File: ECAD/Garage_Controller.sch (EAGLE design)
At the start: 91 parts, among them IC1 LM358D, IC2 LM358D, J1 1885410000, J2 1885410000, J3 1885430000, J4 1885430000, J5 1885430000, J6 1885430000, J7 1885430000, Q1 35A/25V/8.5mΩ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

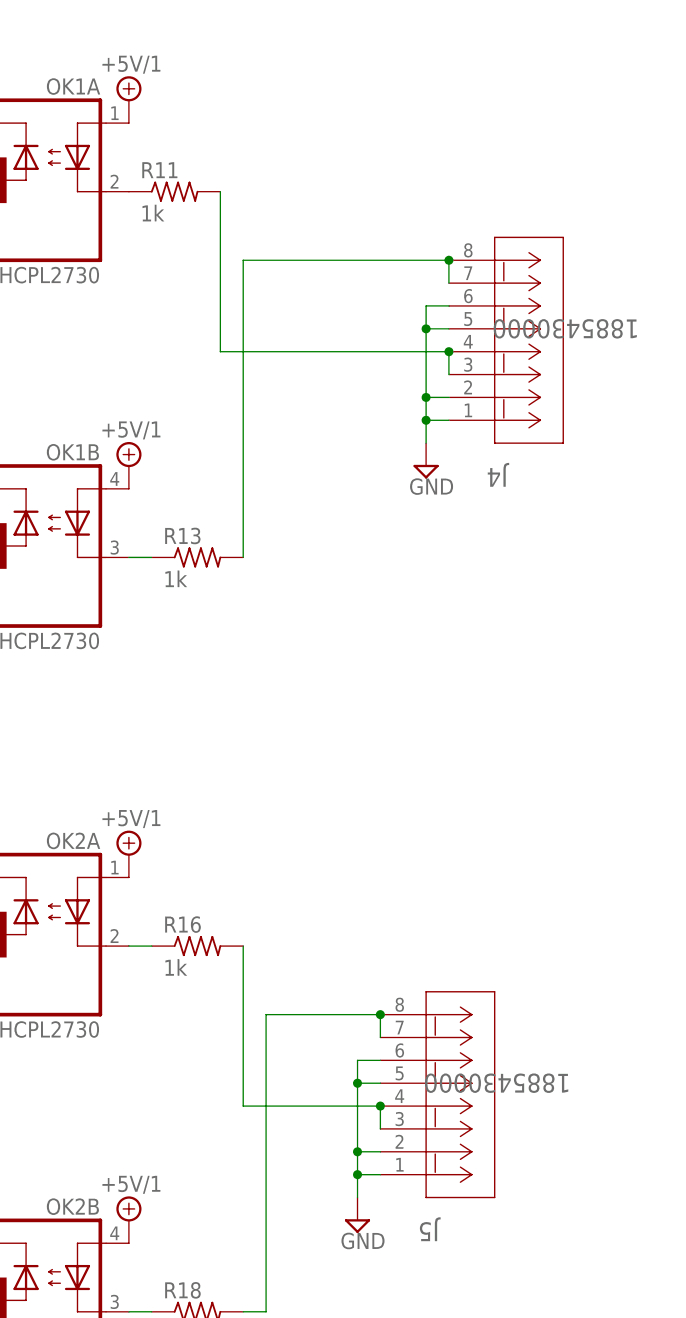
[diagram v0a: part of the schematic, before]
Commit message: Providing +5V at DI connector
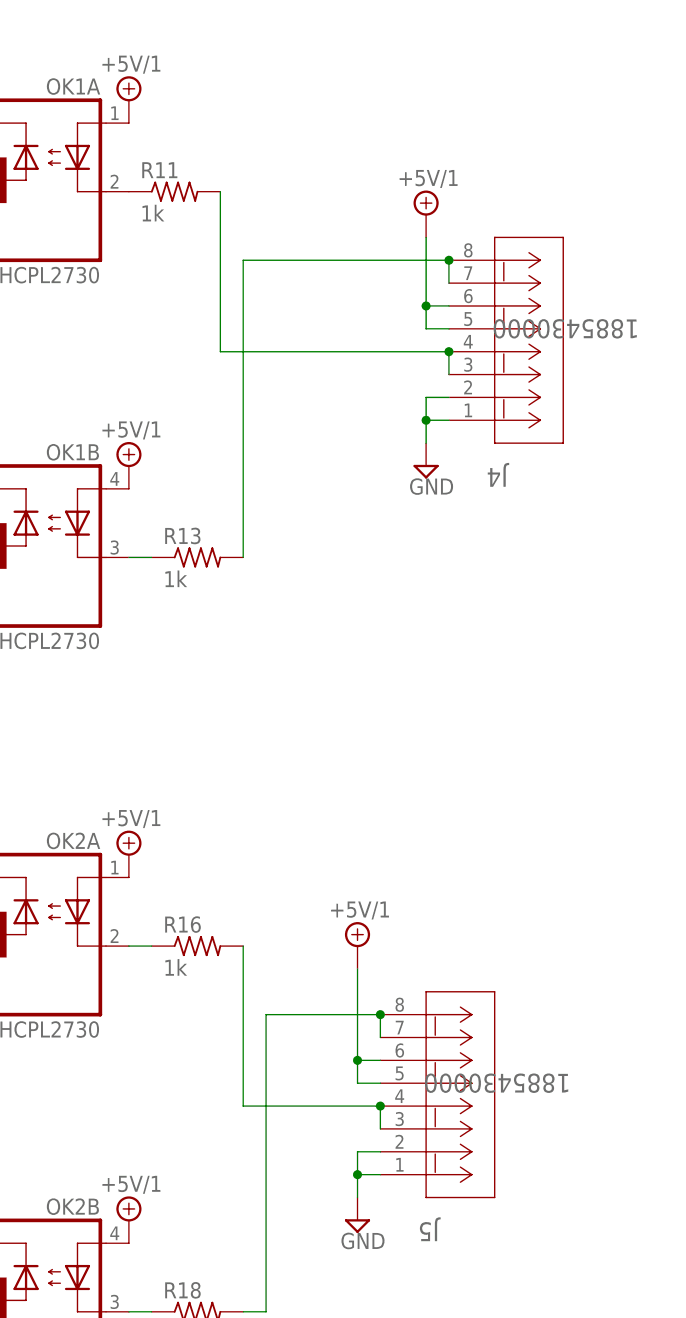
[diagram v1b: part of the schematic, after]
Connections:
- net +5V/1: now also J4.5, J4.6, J5.5, J5.6
- net GND: no longer J4.5, J4.6, J5.5, J5.6
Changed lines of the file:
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@@
 <part name="SUPPLY45" library="supply2" deviceset="GND" device=""/>
 <part name="SUPPLY46" library="supply2" deviceset="+5V" device=""/>
+<part name="SUPPLY47" library="supply2" deviceset="+5V/1" device=""/>
+<part name="SUPPLY48" library="supply2" deviceset="+5V/1" device=""/>
 </parts>
 <sheets>
@@
 <instance part="SUPPLY45" gate="GND" x="297.18" y="175.26"/>
 <instance part="SUPPLY46" gate="+5V" x="297.18" y="198.12"/>
+<instance part="SUPPLY47" gate="G$1" x="325.12" y="-53.34"/>
+<instance part="SUPPLY48" gate="G$1" x="317.5" y="-134.62"/>
 </instances>
 <busses>
@@
 <wire x1="325.12" y1="-73.66" x2="325.12" y2="-76.2" width="0.1524" layer="91"/>
 <junction x="325.12" y="-76.2"/>
-<pinref part="J4" gate="A" pin="5"/>
-<wire x1="327.66" y1="-66.04" x2="325.12" y2="-66.04" width="0.1524" layer="91"/>
-<wire x1="325.12" y1="-66.04" x2="325.12" y2="-73.66" width="0.1524" layer="91"/>
-<junction x="325.12" y="-73.66"/>
-<pinref part="J4" gate="A" pin="6"/>
-<wire x1="327.66" y1="-63.5" x2="325.12" y2="-63.5" width="0.1524" layer="91"/>
-<wire x1="325.12" y1="-63.5" x2="325.12" y2="-66.04" width="0.1524" layer="91"/>
-<junction x="325.12" y="-66.04"/>
 </segment>
 <segment>
@@
 <wire x1="317.5" y1="-157.48" x2="317.5" y2="-160.02" width="0.1524" layer="91"/>
 <junction x="317.5" y="-160.02"/>
-<pinref part="J5" gate="A" pin="5"/>
-<wire x1="320.04" y1="-149.86" x2="317.5" y2="-149.86" width="0.1524" layer="91"/>
-<wire x1="317.5" y1="-149.86" x2="317.5" y2="-157.48" width="0.1524" layer="91"/>
-<junction x="317.5" y="-157.48"/>
-<pinref part="J5" gate="A" pin="6"/>
-<wire x1="320.04" y1="-147.32" x2="317.5" y2="-147.32" width="0.1524" layer="91"/>
-<wire x1="317.5" y1="-147.32" x2="317.5" y2="-149.86" width="0.1524" layer="91"/>
-<junction x="317.5" y="-149.86"/>
 </segment>
 <segment>
@@
 <pinref part="SUPPLY44" gate="G$1" pin="+5V/1"/>
 </segment>
-</net>
+<segment>
+<pinref part="J4" gate="A" pin="5"/>
+<wire x1="327.66" y1="-66.04" x2="325.12" y2="-66.04" width="0.1524" layer="91"/>
+<pinref part="J4" gate="A" pin="6"/>
+<wire x1="327.66" y1="-63.5" x2="325.12" y2="-63.5" width="0.1524" layer="91"/>
+<wire x1="325.12" y1="-63.5" x2="325.12" y2="-66.04" width="0.1524" layer="91"/>
+<pinref part="SUPPLY47" gate="G$1" pin="+5V/1"/>
+<wire x1="325.12" y1="-63.5" x2="325.12" y2="-55.88" width="0.1524" layer="91"/>
+<junction x="325.12" y="-63.5"/>
+</segment>
+<segment>
+<pinref part="J5" gate="A" pin="5"/>
+<wire x1="320.04" y1="-149.86" x2="317.5" y2="-149.86" width="0.1524" layer="91"/>
+<pinref part="J5" gate="A" pin="6"/>
+<wire x1="320.04" y1="-147.32" x2="317.5" y2="-147.32" width="0.1524" layer="91"/>
+<wire x1="317.5" y1="-147.32" x2="317.5" y2="-149.86" width="0.1524" layer="91"/>
+<pinref part="SUPPLY48" gate="G$1" pin="+5V/1"/>
+<wire x1="317.5" y1="-147.32" x2="317.5" y2="-137.16" width="0.1524" layer="91"/>
+<junction x="317.5" y="-147.32"/>
+</segment>
+</net>

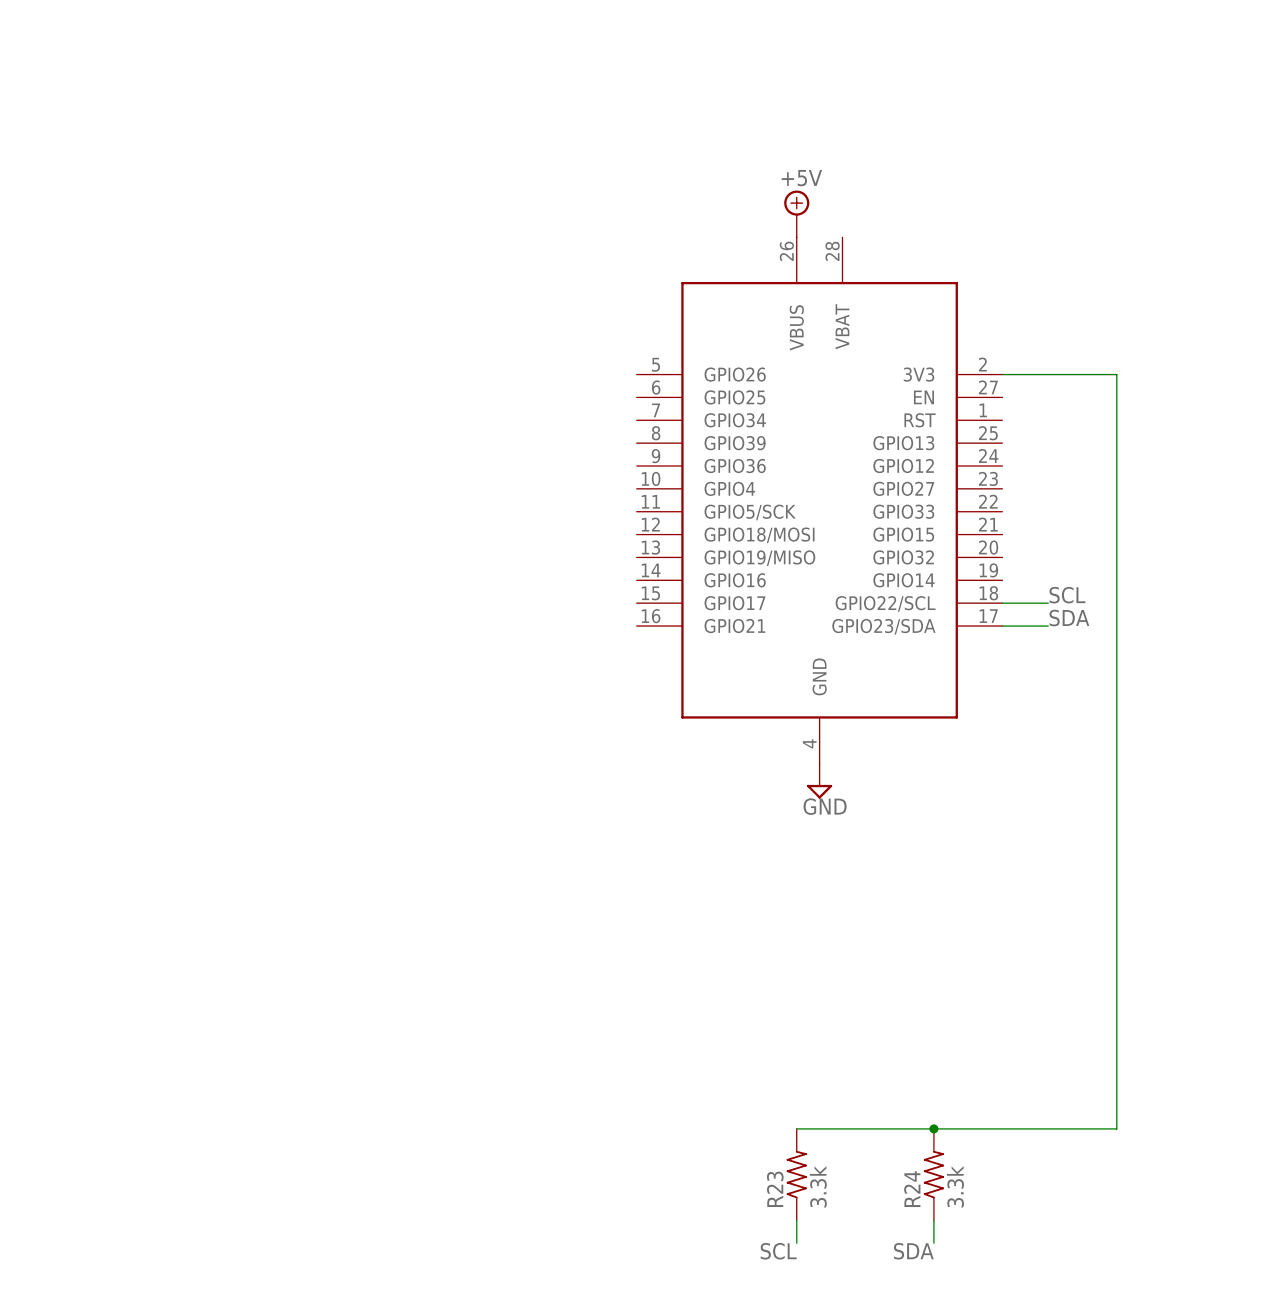
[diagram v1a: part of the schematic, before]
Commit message: Switching to Huzzah ESP8266 breakout
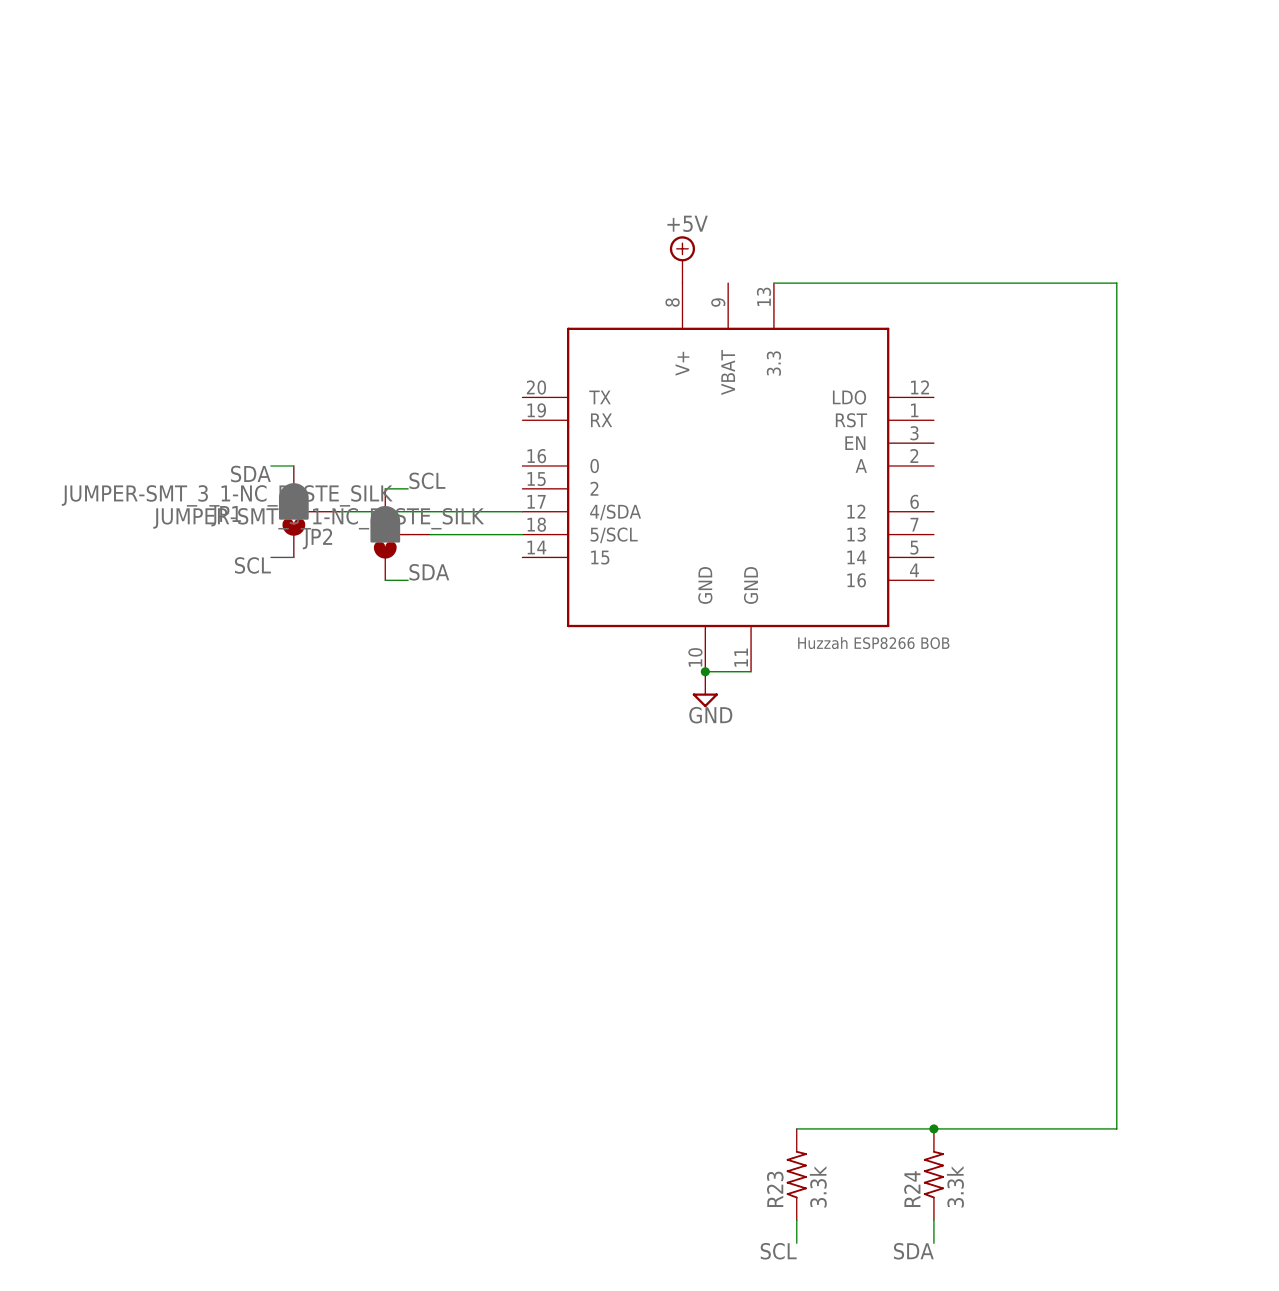
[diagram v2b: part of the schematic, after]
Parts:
- removed U$1: ADAFRUIT_HUZZAH32, FRC696:ADAFRUIT_HUZZAH32
- added JP1, JP2: JUMPER-SMT_3_1-NC_PASTE_SILK, SparkFun-Jumpers:JUMPER-SMT_3_1-NC_PASTE_SILK
- added U$2: HUZZAH_ESP8266_BREAKOUT, adafruit:HUZZAH_ESP8266_BREAKOUT
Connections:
- new net N$39: JP2.2, U$2.5/SCL
- new net N$40: JP1.2, U$2.4/SDA
- net +5V: now also U$2.V+; no longer U$1.VBUS
- net GND: now also U$2.GND@1, U$2.GND@2; no longer U$1.GND
- net N$35: now also U$2.3.3; no longer U$1.3V3
- net SCL: now also JP1.1, JP2.3; no longer U$1.GPIO22/SCL
- net SDA: now also JP1.3, JP2.1; no longer U$1.GPIO23/SDA
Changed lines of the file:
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@@
 </classes>
 <parts>
-<part name="U$1" library="FRC696" deviceset="ADAFRUIT_HUZZAH32" device=""/>
 <part name="SUPPLY1" library="supply2" deviceset="GND" device=""/>
 <part name="SUPPLY2" library="supply2" deviceset="+5V" device=""/>
@@
 <part name="SUPPLY47" library="supply2" deviceset="+5V/1" device=""/>
 <part name="SUPPLY48" library="supply2" deviceset="+5V/1" device=""/>
+<part name="U$2" library="adafruit" deviceset="HUZZAH_ESP8266_BREAKOUT" device=""/>
+<part name="JP1" library="SparkFun-Jumpers" deviceset="JUMPER-SMT_3_1-NC_PASTE" device="_SILK"/>
+<part name="JP2" library="SparkFun-Jumpers" deviceset="JUMPER-SMT_3_1-NC_PASTE" device="_SILK"/>
 </parts>
 <sheets>
@@
 </plain>
 <instances>
-<instance part="U$1" gate="A" x="66.04" y="50.8"/>
-<instance part="SUPPLY1" gate="GND" x="66.04" y="17.78"/>
-<instance part="SUPPLY2" gate="+5V" x="63.5" y="81.28"/>
+<instance part="SUPPLY1" gate="GND" x="53.34" y="27.94"/>
+<instance part="SUPPLY2" gate="+5V" x="50.8" y="76.2"/>
 <instance part="Q1" gate="NMOS" x="248.92" y="88.9"/>
 <instance part="SUPPLY3" gate="GND" x="251.46" y="81.28"/>
@@
 <instance part="SUPPLY47" gate="G$1" x="325.12" y="-53.34"/>
 <instance part="SUPPLY48" gate="G$1" x="317.5" y="-134.62"/>
+<instance part="U$2" gate="A" x="55.88" y="53.34"/>
+<instance part="JP1" gate="G$1" x="7.62" y="48.26" rot="R180"/>
+<instance part="JP2" gate="G$1" x="17.78" y="45.72" rot="R180"/>
 </instances>
 <busses>
@@
 <nets>
 <net name="GND" class="0">
-<segment>
-<pinref part="U$1" gate="A" pin="GND"/>
-<pinref part="SUPPLY1" gate="GND" pin="GND"/>
-</segment>
 <segment>
 <pinref part="Q1" gate="NMOS" pin="S"/>
@@
 <pinref part="SUPPLY45" gate="GND" pin="GND"/>
 </segment>
+<segment>
+<pinref part="U$2" gate="A" pin="GND@1"/>
+<pinref part="SUPPLY1" gate="GND" pin="GND"/>
+<pinref part="U$2" gate="A" pin="GND@2"/>
+<wire x1="53.34" y1="30.48" x2="58.42" y2="30.48" width="0.1524" layer="91"/>
+<junction x="53.34" y="30.48"/>
+</segment>
 </net>
 <net name="+5V" class="0">
-<segment>
-<pinref part="U$1" gate="A" pin="VBUS"/>
-<pinref part="SUPPLY2" gate="+5V" pin="+5V"/>
-</segment>
 <segment>
 <pinref part="U2" gate="G$1" pin="OUT"/>
@@
 <pinref part="R39" gate="G$1" pin="2"/>
 <pinref part="SUPPLY46" gate="+5V" pin="+5V"/>
+</segment>
+<segment>
+<pinref part="U$2" gate="A" pin="V+"/>
+<pinref part="SUPPLY2" gate="+5V" pin="+5V"/>
 </segment>
 </net>
@@
 <net name="SCL" class="0">
 <segment>
-<pinref part="U$1" gate="A" pin="GPIO22/SCL"/>
-<wire x1="86.36" y1="38.1" x2="91.44" y2="38.1" width="0.1524" layer="91"/>
-<label x="91.44" y="38.1" size="1.778" layer="95"/>
-</segment>
-<segment>
 <pinref part="U1" gate="A" pin="SCL"/>
 <wire x1="33.02" y1="-99.06" x2="27.94" y2="-99.06" width="0.1524" layer="91"/>
@@
 <label x="121.92" y="-30.48" size="1.778" layer="95" rot="R180"/>
 </segment>
+<segment>
+<pinref part="JP2" gate="G$1" pin="3"/>
+<wire x1="17.78" y1="50.8" x2="20.32" y2="50.8" width="0.1524" layer="91"/>
+<label x="20.32" y="50.8" size="1.778" layer="95"/>
+</segment>
+<segment>
+<pinref part="JP1" gate="G$1" pin="1"/>
+<wire x1="7.62" y1="43.18" x2="5.08" y2="43.18" width="0.1524" layer="91"/>
+<label x="5.08" y="43.18" size="1.778" layer="95" rot="R180"/>
+</segment>
 </net>
 <net name="SDA" class="0">
-<segment>
-<pinref part="U$1" gate="A" pin="GPIO23/SDA"/>
-<wire x1="86.36" y1="35.56" x2="91.44" y2="35.56" width="0.1524" layer="91"/>
-<label x="91.44" y="35.56" size="1.778" layer="95"/>
-</segment>
 <segment>
 <pinref part="U1" gate="A" pin="SDA"/>
@@
 <wire x1="127" y1="-48.26" x2="121.92" y2="-48.26" width="0.1524" layer="91"/>
 <label x="121.92" y="-48.26" size="1.778" layer="95" rot="R180"/>
+</segment>
+<segment>
+<pinref part="JP1" gate="G$1" pin="3"/>
+<wire x1="7.62" y1="53.34" x2="5.08" y2="53.34" width="0.1524" layer="91"/>
+<label x="5.08" y="53.34" size="1.778" layer="95" rot="R180"/>
+</segment>
+<segment>
+<pinref part="JP2" gate="G$1" pin="1"/>
+<wire x1="17.78" y1="40.64" x2="20.32" y2="40.64" width="0.1524" layer="91"/>
+<label x="20.32" y="40.64" size="1.778" layer="95"/>
 </segment>
 </net>
@@
 <net name="N$35" class="0">
 <segment>
-<pinref part="U$1" gate="A" pin="3V3"/>
-<wire x1="86.36" y1="63.5" x2="99.06" y2="63.5" width="0.1524" layer="91"/>
-<wire x1="99.06" y1="63.5" x2="99.06" y2="-20.32" width="0.1524" layer="91"/>
+<wire x1="99.06" y1="73.66" x2="99.06" y2="-20.32" width="0.1524" layer="91"/>
 <pinref part="R24" gate="G$1" pin="2"/>
 <wire x1="99.06" y1="-20.32" x2="78.74" y2="-20.32" width="0.1524" layer="91"/>
@@
 <wire x1="63.5" y1="-20.32" x2="78.74" y2="-20.32" width="0.1524" layer="91"/>
 <junction x="78.74" y="-20.32"/>
+<pinref part="U$2" gate="A" pin="3.3"/>
+<wire x1="60.96" y1="73.66" x2="99.06" y2="73.66" width="0.1524" layer="91"/>
 </segment>
 </net>
@@
 </segment>
 </net>
+<net name="N$39" class="0">
+<segment>
+<pinref part="U$2" gate="A" pin="5/SCL"/>
+<pinref part="JP2" gate="G$1" pin="2"/>
+<wire x1="33.02" y1="45.72" x2="22.86" y2="45.72" width="0.1524" layer="91"/>
+</segment>
+</net>
+<net name="N$40" class="0">
+<segment>
+<pinref part="U$2" gate="A" pin="4/SDA"/>
+<pinref part="JP1" gate="G$1" pin="2"/>
+<wire x1="33.02" y1="48.26" x2="12.7" y2="48.26" width="0.1524" layer="91"/>
+</segment>
+</net>
